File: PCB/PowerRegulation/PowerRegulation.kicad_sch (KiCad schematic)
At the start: 94 parts, among them J1 USB_C_Receptacle_USB2.0_14P, SW1 RESET, SW2 RESET, U1 BQ25883RGER, U10 MCP4651-503E/ST, U11 PAM8403, U3 STM32F072CBTx, U5 TPS563200DDCR, U6 TPS563200DDCR, U7 TPS563200DDCR, U8 TPS563200DDCR, U9 TPS563200DDCR

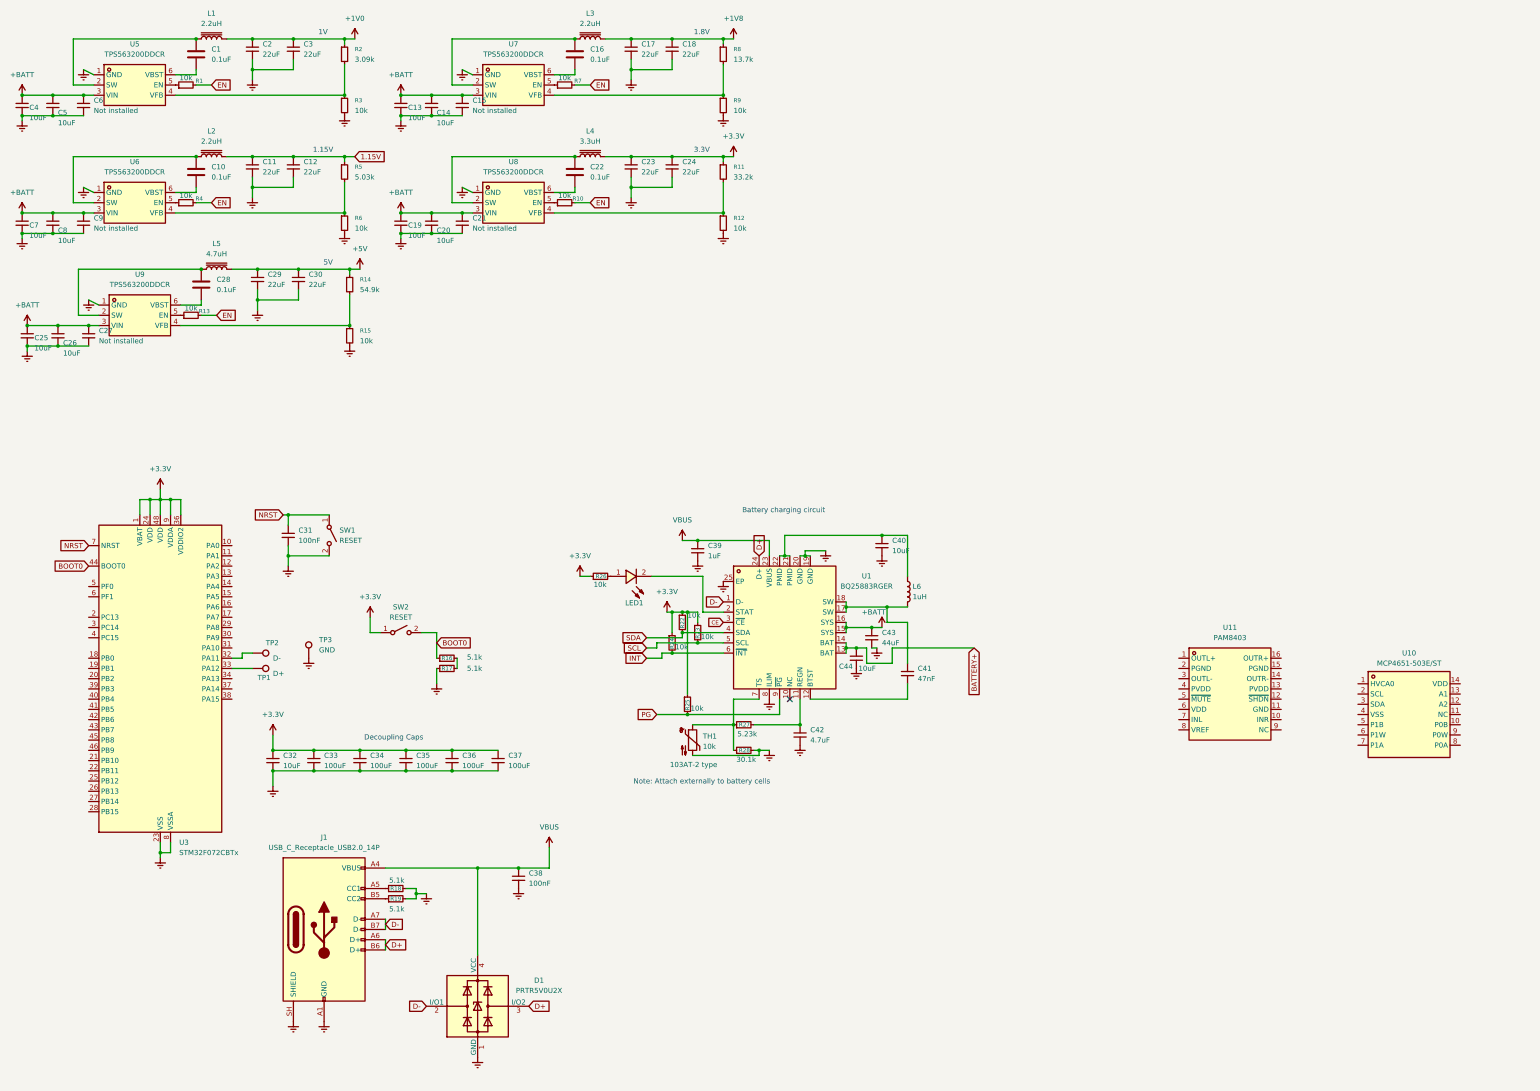
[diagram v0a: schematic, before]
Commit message: finsh the speaker amp and digital potentiometer
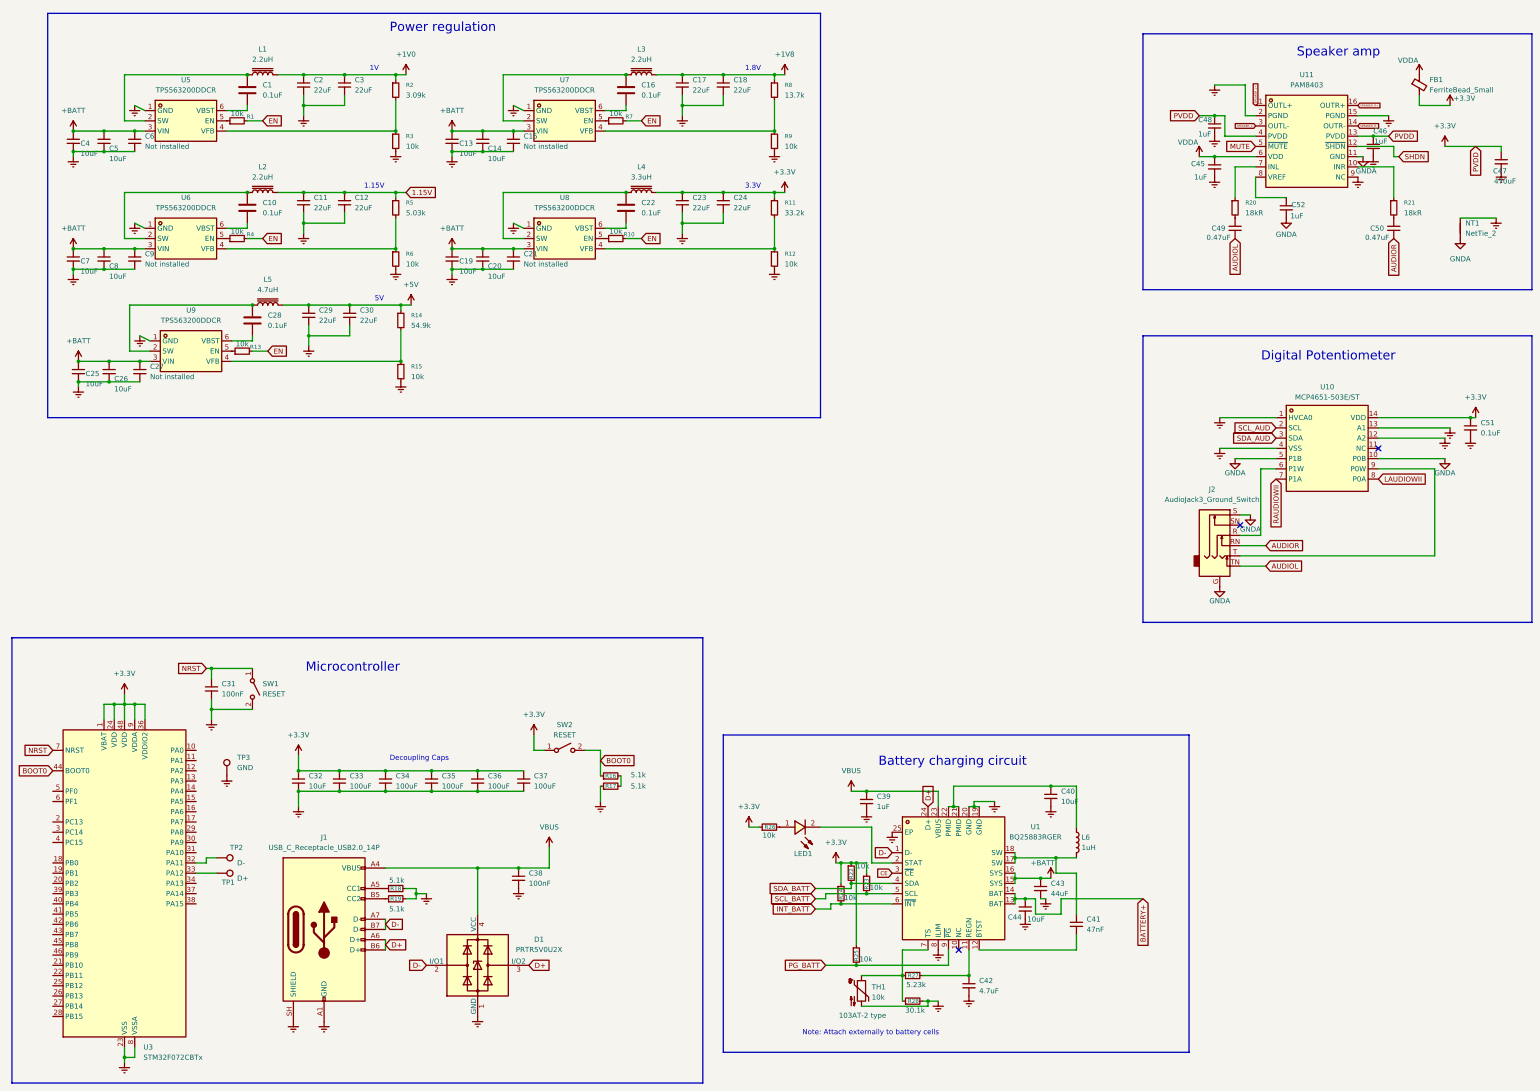
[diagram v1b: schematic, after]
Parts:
- added C45, C46, C48, C52: 1uF, symbol Device:C_Small
- added C47: 470uF, symbol Device:C_Small
- added C49, C50: 0.47uF, symbol Device:C_Small
- added C51: 0.1uF, symbol Device:C_Small
- added FB1: FerriteBead_Small, symbol Device:FerriteBead_Small
- added J2: AudioJack3_Ground_Switch, symbol Connector_Audio:AudioJack3_Ground_Switch
- added NT1: NetTie_2, symbol Device:NetTie_2
- added R20, R21: 18kR, symbol Device:R_Small
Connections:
- net +3.3V: now also U10.14 (VDD), U11.13 (PVDD), U11.4 (PVDD), C46.1, C47.1, C48.1, C51.1, FB1.2
- net GNDREF: now also U10.1 (HVCA0), U10.12 (A2), U10.13 (A1), U10.4 (VSS), U11.15 (PGND), U11.2 (PGND), U11.9 (NC), C45.2, C46.2, C47.2, C48.2, C51.2, NT1.2
- net GNDA: now reaches U10.10 (P0B)
- net GNDA: now also U10.5 (P1B), U11.11 (GND), C52.2, J2.G, J2.S, NT1.1
- net SCL_AUD: now reaches U10.2 (SCL)
- net SDA_AUD: now reaches U10.3 (SDA)
- net at U10.6 (P1W): now also J2.R
- net RAUDIOWII: now reaches U10.7 (P1A)
- net LAUDIOWII: now reaches U10.8 (P0A)
- net at U10.9 (P0W): now also J2.T
- net SPEAKER_L+: now reaches U11.1 (OUTL+)
- net at U11.10 (INR): now also R21.1
- net SHDN: now reaches U11.12 (~{SHDN})
- net SPEAKER_R-: now reaches U11.14 (OUTR-)
- net SPEAKER_R+: now reaches U11.16 (OUTR+)
- net SPEAKER_L-: now reaches U11.3 (OUTL-)
- net MUTE: now reaches U11.5 (~{MUTE})
- net VDDA: now reaches U11.6 (VDD)
- net VDDA: now also C45.1, FB1.1
- net at U11.7 (INL): now also R20.1
- net at U11.8 (VREF): now also C52.1
- net INT renamed INT_BATT
- net PG renamed PG_BATT
- net SCL renamed SCL_BATT
- net SDA renamed SDA_BATT
- new net: C49.1, R20.2
- new net: C50.1, R21.2
- new net AUDIOL: C49.2, J2.TN
- new net AUDIOR: C50.2, J2.RN
- no-connect marks 1 -> 3
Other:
- note added: "Digital Potentiometer"
- note added: "Microcontroller"
- note added: "Power regulation"
- note added: "Speaker amp"
- moved on the sheet: C1, C10, C11, C12, C13, C14, C15, C16, C17, C18, C19, C2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

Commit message: Complete oled connections and start assigning footprints to symbols
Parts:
- removed C47: 470uF, symbol Device:C_Small
- added C47: 470uF, EasyEDA:CAP-SMD_BD8.0-L8.3-W8.3-FD, symbol Device:C_Polarized_Small
- added C53: 22uF, EasyEDA:R1206, symbol Device:C_Small
- added J3: Wii audio in, Connector_PinHeader_2.54mm:PinHeader_1x03_P2.54mm_Vertical, symbol Connector:Conn_01x03_Pin
- added J4: OLED, symbol Connector_Generic:Conn_01x04
- added TP4: GND, Connector_Pin:Pin_D1.1mm_L8.5mm_W2.5mm_FlatFork, symbol Connector:TestPoint
- added TP5: 1V, Connector_Pin:Pin_D1.1mm_L8.5mm_W2.5mm_FlatFork, symbol Connector:TestPoint
- added TP6: 1.15V, Connector_Pin:Pin_D1.1mm_L8.5mm_W2.5mm_FlatFork, symbol Connector:TestPoint
- added TP7: 1.8V, Connector_Pin:Pin_D1.1mm_L8.5mm_W2.5mm_FlatFork, symbol Connector:TestPoint
- added TP8: 3.3V, Connector_Pin:Pin_D1.1mm_L8.5mm_W2.5mm_FlatFork, symbol Connector:TestPoint
- added TP9: 5V, Connector_Pin:Pin_D1.1mm_L8.5mm_W2.5mm_FlatFork, symbol Connector:TestPoint
- C1, C10, C16, C22, C28, C31, C38, C39, C41, C45, C46, C48, C49, C50, C51, C52, L6, R14, R2, R8: footprint (none) -> EasyEDA:R0603
- C11, C12, C17, C18, C2, C23, C24, C29, C3, C30, R1, R10, R12, R13, R15, R22, R23, R24, R25, R26, R3, R4, R6, R7, R9: footprint (none) -> EasyEDA:R1206
- C13, C14, C15, C19, C20, C21, C25, C26, C27, C32, C4, C40, C42, C44, C5, C6, C7, C8, C9, R11: footprint (none) -> EasyEDA:R0805
- C33, C34, C35, C36, C37: value 100uF -> 100nF; footprint (none) -> EasyEDA:R0603
- C43: value 44uF -> 22uF; footprint (none) -> EasyEDA:R1206
- L1, L2, L3: footprint (none) -> EasyEDA:IND-SMD_L4.5-W4.1_SRP4020TA
- L4: footprint (none) -> EasyEDA:IND-SMD_L5.7-W5.2
- L5: footprint Inductor_SMD:L_0402_1005Metric -> EasyEDA:IND-SMD_L7.1-W6.6
- U3: footprint Package_QFP:LQFP-48_7x7mm_P0.5mm -> EasyEDA:LQFP-48_L7.0-W7.0-P0.50-LS9.0-BL
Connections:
- net +1V0: now also TP5.1
- net +1V8: now also TP7.1
- net +3.3V: now also C47.1, TP8.1
- net +5V: now also TP9.1
- net +BATT: now also C53.1
- net 1.15V: now also TP6.1
- net EN: now also U3.40 (PB4)
- net GNDA: now also J3.1 (GND)
- net GNDREF: now also C47.2, C53.2, TP4.1
- net INT_BATT: now also U3.18 (PB0)
- net LAUDIOWII: now also J3.2 (Left)
- net MUTE: now also U3.20 (PB2)
- net PG_BATT: now also U3.19 (PB1)
- net RAUDIOWII: now also J3.3 (Right)
- net SCL_AUD: now also U3.26 (PB13)
- net SCL_BATT: now also U3.42 (PB6)
- net SDA_AUD: now also U3.27 (PB14)
- net SDA_BATT: now also U3.43 (PB7)
- net SHDN: now also U3.39 (PB3)
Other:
- note added: "Microcontroller & OLED"
- note removed: "Microcontroller"
- moved on the sheet: C38, C39, C40, C41, C42, C43, C44, C51, D1, J1, J2, L6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

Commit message: Finish the Schematic
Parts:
- removed C47: 470uF, EasyEDA:CAP-SMD_BD8.0-L8.3-W8.3-FD, symbol Device:C_Polarized_Small
- removed L6: 1uH, EasyEDA:R0603, symbol Device:L
- added C47: RVT1V470M0605, EasyEDA:CAP-SMD_BD6.3-L6.6-W6.6-LS7.2-FD, symbol EasyEDA:RVT1V470M0605
- added C54, C56: 10nF, EasyEDA:R1206, symbol Device:C_Small
- added C55, C57: 1uF, EasyEDA:R1206, symbol Device:C_Small
- added C58, C59: 0.1uF, EasyEDA:R1206, symbol Device:C_Small
- added L6: 1uH, EasyEDA:IND-SMD_L5.4-W5.2_PSPMAA0503, symbol EasyEDA:PSPMAA0503-1R0M-ANP
- added R29, R30: 4.7k, EasyEDA:R0805, symbol Device:R_Small
- added R31, R32: 10k, EasyEDA:R1206, symbol Device:R_Small
- added TP10: B+, TestPoint:TestPoint_Pad_D3.0mm, symbol Connector:TestPoint
- added TP11: B-, TestPoint:TestPoint_Pad_D3.0mm, symbol Connector:TestPoint
- added U2, U4: TPS22918DBVR, EasyEDA:SOT-23-6_L2.9-W1.6-P0.95-LS2.8-BR, symbol EasyEDA:TPS22918DBVR
- FB1, R20, R21: footprint (none) -> EasyEDA:R0805
- J1: footprint (none) -> EasyEDA:USB-C-SMD_TYPE-C-16PIN-2MD-073
- J4: footprint (none) -> Connector_PinHeader_2.54mm:PinHeader_1x04_P2.54mm_Vertical
- NT1: footprint (none) -> NetTie:NetTie-2_SMD_Pad2.0mm
- R16, R17, R18, R19, R27, R5: footprint (none) -> EasyEDA:R0603
- R26: value 10k -> 470R; footprint EasyEDA:R1206 -> EasyEDA:R0805
- R28, TH1: footprint (none) -> EasyEDA:R1206
- SW2: value RESET -> BOOT
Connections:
- net +3.3V: now also J4.VCC (Pin_1), C57.1, R29.1, R30.1, U2.1 (VIN); no longer C46.1, C48.1, TP8.1, U11.13 (PVDD), U11.4 (PVDD)
- net +5V: now also C46.1, C48.1, U11.13 (PVDD), U11.4 (PVDD), C47.1, C55.1, U4.1 (VIN); no longer TP9.1
- net +BATT: now also R10.2, R13.2
- net BATTERY+: now also TP10.1
- net EN: now also U2.3 (ON), U4.3 (ON); no longer R10.2, R13.2
- net GNDREF: now also J4.GND (Pin_2), C47.2, C54.2, C55.2, C56.2, C57.2, C58.2, C59.2, R31.2, R32.2, TP11.1, U2.2 (GND), U4.2 (GND)
- net MUTE: now also R32.1
- net SCL_AUD: now also R30.2
- net SDA_AUD: now also R29.2
- net SHDN: now also R31.1
- net at C40.1, U1.21 (PMID), U1.22 (PMID): now also L6.1
- net at J4.SCL (Pin_4): now also U3.16 (PA6)
- net at J4.SDA (Pin_3): now also U3.15 (PA5)
- net at C41.1, U1.17 (SW), U1.18 (SW): now also L6.2
- new net: C58.1, TP8.1, U2.5 (QOD), U2.6 (VOUT)
- new net: C59.1, TP9.1, U4.5 (QOD), U4.6 (VOUT)
- new net: C54.1, U4.4 (CT)
- new net: C56.1, U2.4 (CT)
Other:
- moved on the sheet: C31, C32, C33, C34, C35, C36, C37, J4, R16, R17, SW1, SW2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

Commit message: layout the mcu and battery charging circuits
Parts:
- TP10, TP11: footprint TestPoint:TestPoint_Pad_D3.0mm -> TestPoint:TestPoint_Pad_D4.0mm
- TP4, TP5, TP6, TP7, TP8, TP9: footprint Connector_Pin:Pin_D1.1mm_L8.5mm_W2.5mm_FlatFork -> TestPoint:TestPoint_Pad_D4.0mm
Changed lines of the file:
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@@
 			)
 		)
-		(property "Footprint" "Connector_Pin:Pin_D1.1mm_L8.5mm_W2.5mm_FlatFork"
+		(property "Footprint" "TestPoint:TestPoint_Pad_D4.0mm"
 			(at 146.05 95.25 0)
 			(hide yes)
@@
 			)
 		)
-		(property "Footprint" "Connector_Pin:Pin_D1.1mm_L8.5mm_W2.5mm_FlatFork"
+		(property "Footprint" "TestPoint:TestPoint_Pad_D4.0mm"
 			(at 162.56 95.25 0)
 			(hide yes)
@@
 			)
 		)
-		(property "Footprint" "TestPoint:TestPoint_Pad_D3.0mm"
+		(property "Footprint" "TestPoint:TestPoint_Pad_D4.0mm"
 			(at 281.94 240.03 0)
 			(hide yes)
@@
 			)
 		)
-		(property "Footprint" "Connector_Pin:Pin_D1.1mm_L8.5mm_W2.5mm_FlatFork"
+		(property "Footprint" "TestPoint:TestPoint_Pad_D4.0mm"
 			(at 219.71 105.41 0)
 			(hide yes)
@@
 			)
 		)
-		(property "Footprint" "TestPoint:TestPoint_Pad_D3.0mm"
+		(property "Footprint" "TestPoint:TestPoint_Pad_D4.0mm"
 			(at 297.18 240.03 0)
 			(hide yes)
@@
 			)
 		)
-		(property "Footprint" "Connector_Pin:Pin_D1.1mm_L8.5mm_W2.5mm_FlatFork"
+		(property "Footprint" "TestPoint:TestPoint_Pad_D4.0mm"
 			(at 172.72 95.25 0)
 			(hide yes)
@@
 			)
 		)
-		(property "Footprint" "Connector_Pin:Pin_D1.1mm_L8.5mm_W2.5mm_FlatFork"
+		(property "Footprint" "TestPoint:TestPoint_Pad_D4.0mm"
 			(at 170.18 115.57 0)
 			(hide yes)
@@
 			)
 		)
-		(property "Footprint" "Connector_Pin:Pin_D1.1mm_L8.5mm_W2.5mm_FlatFork"
+		(property "Footprint" "TestPoint:TestPoint_Pad_D4.0mm"
 			(at 153.67 95.25 0)
 			(hide yes)
